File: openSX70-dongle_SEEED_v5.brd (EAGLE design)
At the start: 100.5 x 53.4 mm, 24 parts, among them SW1 MK-12C02 G1.5, SW2 MK-12C02 G1.5, X1 1503_02

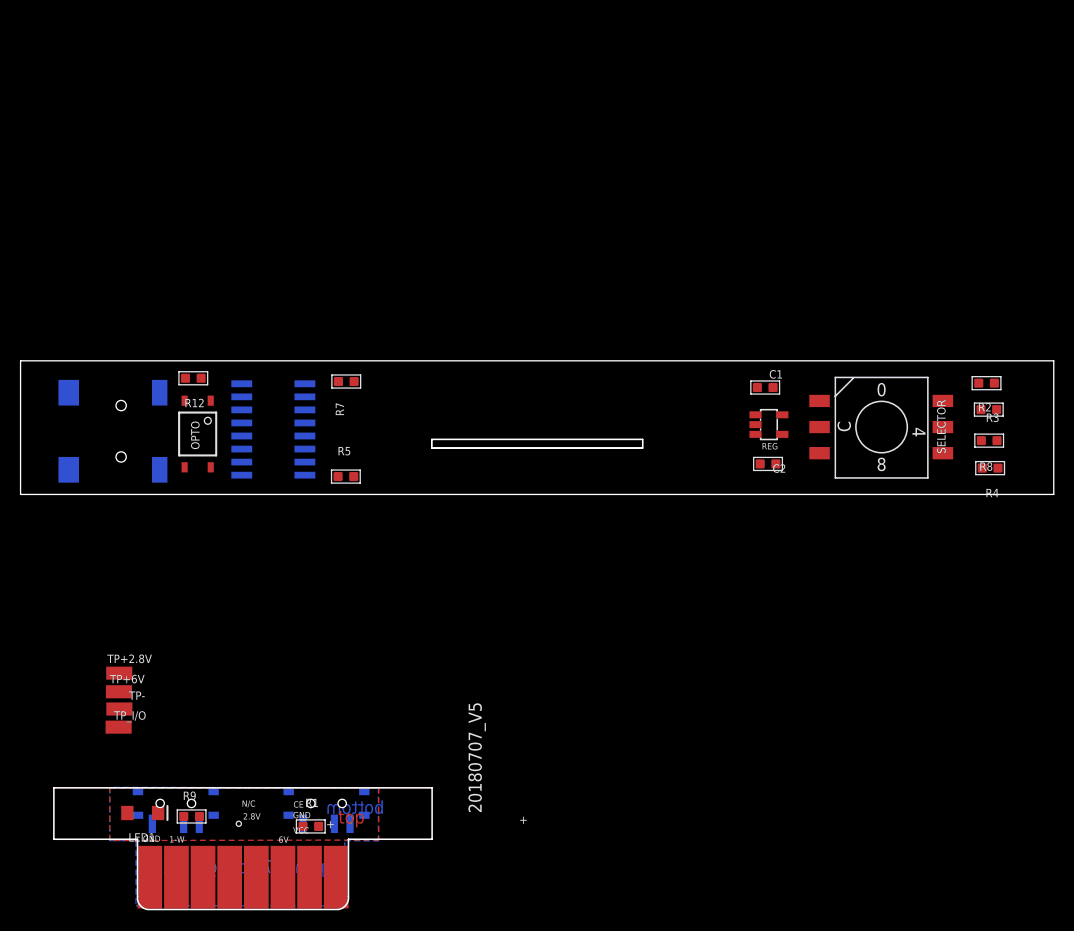
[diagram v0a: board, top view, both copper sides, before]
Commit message: NEW dimensions DXF
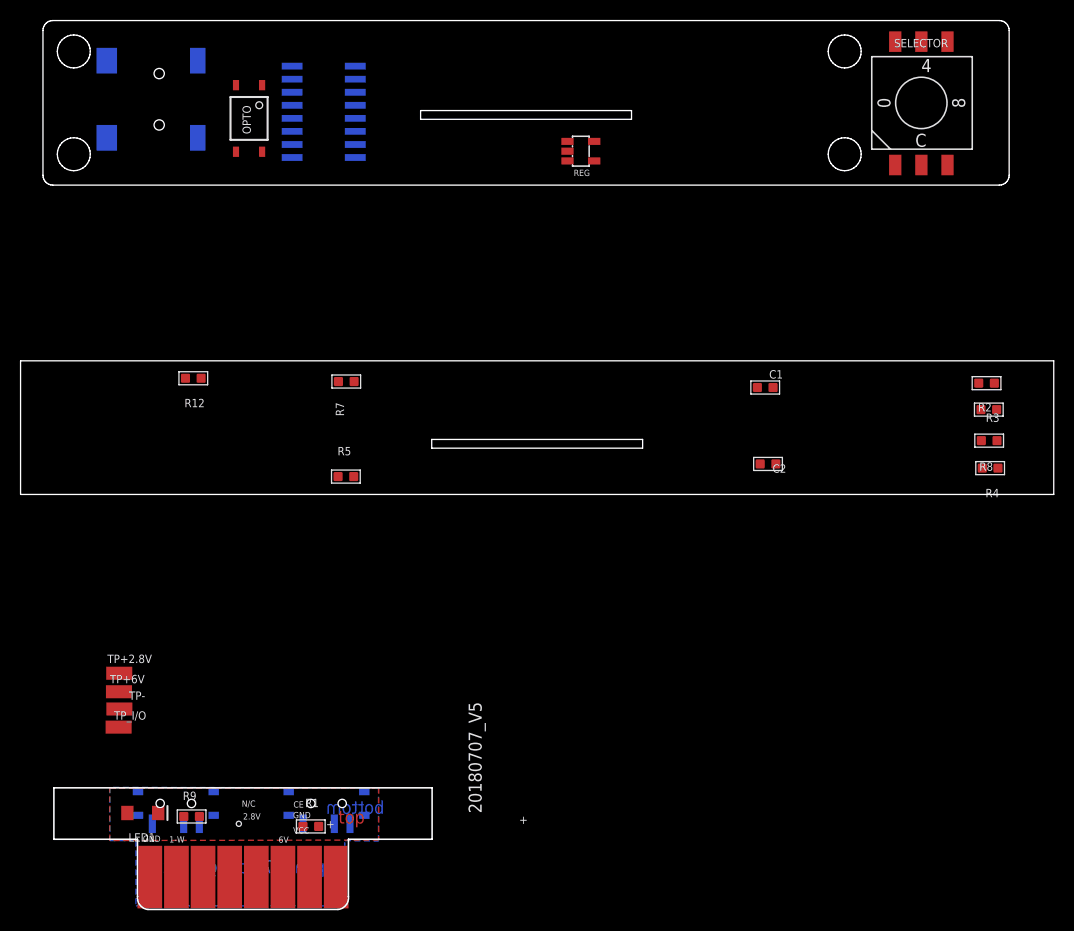
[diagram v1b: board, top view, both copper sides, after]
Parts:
- moved X1 32.5 mm to (10.5, 79.7)
- moved REG 32.3 mm to (58.5, 74.7)
- moved SELECTOR 31.8 mm to (91.7, 79.4), turned to 90 degrees
- moved DS2408 31.3 mm to (33.5, 78.5)
- moved OPTO 31.1 mm to (26.9, 77.9)
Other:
- board size 100.5 x 53.4 mm -> 100.5 x 86.5 mm
